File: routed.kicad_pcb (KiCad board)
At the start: 2 copper layers, 147.2 x 100.3 mm, 56 parts

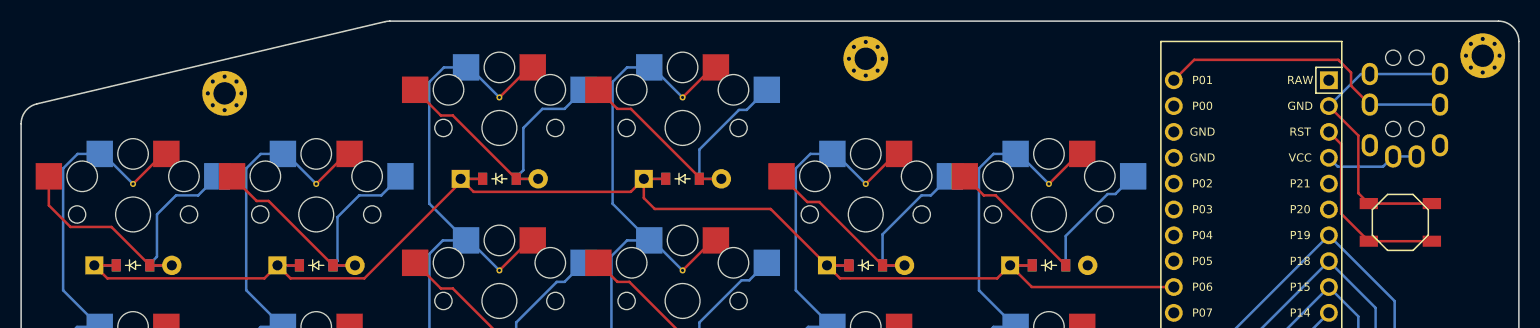
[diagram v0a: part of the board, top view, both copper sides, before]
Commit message: routed.kicad_pcb: fix trrs connections, unconnected diodes [bugfix]
Connected serial data pin P1 of Arduino to pin 2 of TRRS jack, rather
than pin 3 of TRRS jack. Using pin 2 for the serial data will allow
the use of both TRS and TRRS cables, whereas the former use of pin 3
would only work with TRRS cables.

Connect some diode pads that I forgot to connect (thanks, Design Rules
Checker).
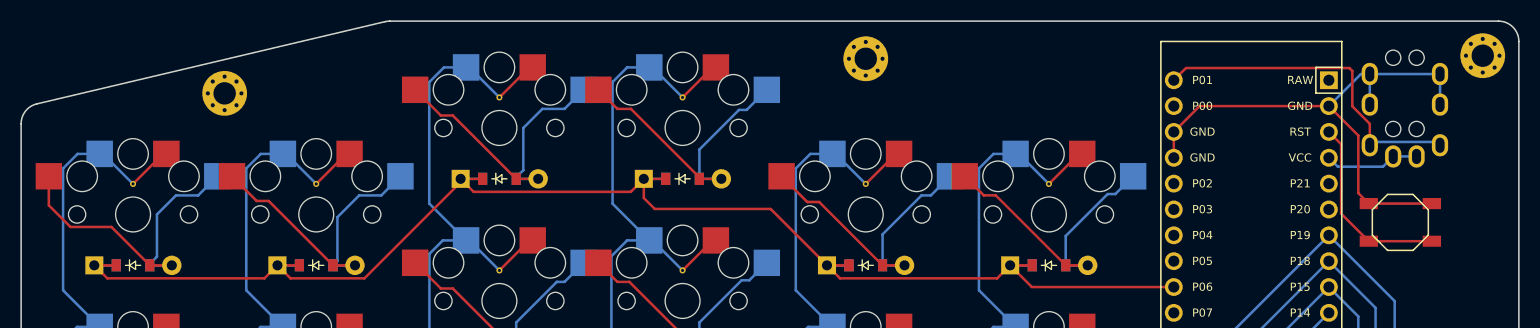
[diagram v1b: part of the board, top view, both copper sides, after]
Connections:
- TRRS1 pad 2: NA -> P1
- TRRS1 pad 3: P1 -> GND
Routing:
- net GND: track 29.6 -> 54.5 mm
- net inner_top: track 25.5 -> 29.8 mm
- net P1: track 29.6 -> 33.3 mm
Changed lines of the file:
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@@
   (net 36 "P5")
   (net 37 "P7")
-  (net 38 "NA")
   (footprint "E73:SW_TACT_ALPS_SKQGABE010" (layer "F.Cu")
     (at 192.286307 79.234243)
@@
     (at 193.8863 61.454246)
     (attr through_hole)
-    (fp_text reference "TRRS1" (at 0 14.2) (layer "Dwgs.User")
-      (effects (font (size 1 1) (thickness 0.15)))
-    )
-    (fp_text value "TRRS-PJ-320A-dual" (at 0 -5.6) (layer "F.Fab")
+    (fp_text reference "TRRS1" (at 6.399047 7.24677) (layer "Dwgs.User")
+      (effects (font (size 1 1) (thickness 0.15)))
+    )
+    (fp_text value "TRRS-PJ-320A-dual" (at 4.800308 12.920066 270) (layer "F.Fab") hide
       (effects (font (size 1 1) (thickness 0.15)))
     )
@@
     (fp_line (start -5.35 0) (end -5.35 12.1) (layer "Dwgs.User") (width 0.15))
     (fp_line (start 0.75 0) (end -5.35 0) (layer "Dwgs.User") (width 0.15))
-    (pad "" np_thru_hole circle locked (at -2.3 8.6) (size 1.5 1.5) (drill 1.5) (layers *.Cu *.Mask))
-    (pad "" np_thru_hole circle locked (at -2.3 1.6) (size 1.5 1.5) (drill 1.5) (layers *.Cu *.Mask))
-    (pad "" np_thru_hole circle locked (at 0 8.6) (size 1.5 1.5) (drill 1.5) (layers *.Cu *.Mask))
-    (pad "" np_thru_hole circle locked (at 0 1.6) (size 1.5 1.5) (drill 1.5) (layers *.Cu *.Mask))
-    (pad "1" thru_hole oval locked (at -2.3 11.3) (size 1.6 2.2) (drill oval 0.9 1.5) (layers *.Cu *.Mask)
+    (pad "" np_thru_hole circle (at -2.3 8.6) (size 1.5 1.5) (drill 1.5) (layers *.Cu *.Mask))
+    (pad "" np_thru_hole circle (at -2.3 1.6) (size 1.5 1.5) (drill 1.5) (layers *.Cu *.Mask))
+    (pad "" np_thru_hole circle (at 0 8.6) (size 1.5 1.5) (drill 1.5) (layers *.Cu *.Mask))
+    (pad "" np_thru_hole circle (at 0 1.6) (size 1.5 1.5) (drill 1.5) (layers *.Cu *.Mask))
+    (pad "1" thru_hole oval (at -2.3 11.3) (size 1.6 2.2) (drill oval 0.9 1.5) (layers *.Cu *.Mask)
       (net 28 "VCC"))
-    (pad "1" thru_hole oval locked (at 0 11.3) (size 1.6 2.2) (drill oval 0.9 1.5) (layers *.Cu *.Mask)
+    (pad "1" thru_hole oval (at 0 11.3) (size 1.6 2.2) (drill oval 0.9 1.5) (layers *.Cu *.Mask)
       (net 28 "VCC"))
-    (pad "2" thru_hole oval locked (at -4.6 10.2) (size 1.6 2.2) (drill oval 0.9 1.5) (layers *.Cu *.Mask)
-      (net 38 "NA"))
-    (pad "2" thru_hole oval locked (at 2.3 10.2) (size 1.6 2.2) (drill oval 0.9 1.5) (layers *.Cu *.Mask)
-      (net 38 "NA"))
-    (pad "3" thru_hole oval locked (at -4.6 6.2) (size 1.6 2.2) (drill oval 0.9 1.5) (layers *.Cu *.Mask)
+    (pad "2" thru_hole oval (at -4.6 10.2) (size 1.6 2.2) (drill oval 0.9 1.5) (layers *.Cu *.Mask)
       (net 31 "P1"))
-    (pad "3" thru_hole oval locked (at 2.3 6.2) (size 1.6 2.2) (drill oval 0.9 1.5) (layers *.Cu *.Mask)
+    (pad "2" thru_hole oval (at 2.3 10.2) (size 1.6 2.2) (drill oval 0.9 1.5) (layers *.Cu *.Mask)
       (net 31 "P1"))
-    (pad "4" thru_hole oval locked (at -4.6 3.2) (size 1.6 2.2) (drill oval 0.9 1.5) (layers *.Cu *.Mask)
+    (pad "3" thru_hole oval (at -4.6 6.2) (size 1.6 2.2) (drill oval 0.9 1.5) (layers *.Cu *.Mask)
       (net 26 "GND"))
-    (pad "4" thru_hole oval locked (at 2.3 3.2) (size 1.6 2.2) (drill oval 0.9 1.5) (layers *.Cu *.Mask)
+    (pad "3" thru_hole oval (at 2.3 6.2) (size 1.6 2.2) (drill oval 0.9 1.5) (layers *.Cu *.Mask)
+      (net 26 "GND"))
+    (pad "4" thru_hole oval (at -4.6 3.2) (size 1.6 2.2) (drill oval 0.9 1.5) (layers *.Cu *.Mask)
+      (net 26 "GND"))
+    (pad "4" thru_hole oval (at 2.3 3.2) (size 1.6 2.2) (drill oval 0.9 1.5) (layers *.Cu *.Mask)
       (net 26 "GND"))
   )
@@
   (gr_line (start 203.936299 61.454246) (end 203.936298 120.464232) (layer "Edge.Cuts") (width 0.15))
   (gr_arc (start 92.529629 59.50777) (mid 92.757869 59.467675) (end 92.989214 59.454245) (layer "Edge.Cuts") (width 0.15))
-  (gr_arc (start 56.756299 69.537017) (mid 57.18799 68.295877) (end 58.296716 67.590538) (layer "Edge.Cuts") (width 0.15))
+  (gr_arc (start 56.756299 69.537017) (mid 57.187989 68.295878) (end 58.296716 67.590538) (layer "Edge.Cuts") (width 0.15))
   (gr_line (start 175.092974 159.612011) (end 126.434172 136.759156) (layer "Edge.Cuts") (width 0.15))
-  (gr_arc (start 201.9363 59.454247) (mid 203.350515 60.040032) (end 203.936299 61.454246) (layer "Edge.Cuts") (width 0.15))
+  (gr_arc (start 201.9363 59.454247) (mid 203.350515 60.040031) (end 203.936299 61.454246) (layer "Edge.Cuts") (width 0.15))
   (gr_line (start 58.296716 67.590538) (end 92.529629 59.50777) (layer "Edge.Cuts") (width 0.15))
   (gr_line (start 126.392648 136.740234) (end 57.94761 106.480919) (layer "Edge.Cuts") (width 0.15))
@@
   (segment (start 160.106299 99.604248) (end 160.106297 95.452312) (width 0.25) (layer "B.Cu") (net 17))
   (segment (start 160.106297 95.452312) (end 161.979848 93.578763) (width 0.25) (layer "B.Cu") (net 17))
+  (segment (start 161.566301 83.454246) (end 159.406301 83.454246) (width 0.25) (layer "F.Cu") (net 18))
   (segment (start 151.355819 76.578762) (end 149.481299 74.704244) (width 0.25) (layer "F.Cu") (net 18))
   (segment (start 152.530822 76.578765) (end 151.355819 76.578762) (width 0.25) (layer "F.Cu") (net 18))
@@
   (segment (start 159.4063 80.571233) (end 163.529915 76.447618) (width 0.25) (layer "B.Cu") (net 18))
   (segment (start 164.287926 76.447618) (end 166.031298 74.704244) (width 0.25) (layer "B.Cu") (net 18))
+  (segment (start 161.566301 83.454246) (end 159.406301 83.454246) (width 0.25) (layer "B.Cu") (net 18))
   (segment (start 159.406302 83.454245) (end 159.4063 80.571233) (width 0.25) (layer "B.Cu") (net 18))
   (segment (start 142.142384 135.269978) (end 140.055984 134.710928) (width 0.25) (layer "F.Cu") (net 19))
@@
   (segment (start 154.255094 138.515567) (end 152.168696 137.956517) (width 0.25) (layer "B.Cu") (net 24))
   (segment (start 171.308444 147.37509) (end 169.781093 145.847737) (width 0.25) (layer "B.Cu") (net 24))
+  (segment (start 170.026296 70.344249) (end 172.566296 67.804249) (width 0.25) (layer "F.Cu") (net 26))
   (segment (start 189.186303 77.384248) (end 188.161782 76.359729) (width 0.25) (layer "F.Cu") (net 26))
+  (segment (start 172.566296 67.804249) (end 185.266296 67.804249) (width 0.25) (layer "F.Cu") (net 26))
   (segment (start 188.161782 76.359729) (end 188.161779 70.699727) (width 0.25) (layer "F.Cu") (net 26))
   (segment (start 189.186303 77.384248) (end 195.386304 77.384243) (width 0.25) (layer "F.Cu") (net 26))
+  (segment (start 170.026296 72.884249) (end 170.026296 70.344249) (width 0.25) (layer "F.Cu") (net 26))
   (segment (start 188.161779 70.699727) (end 185.266298 67.804245) (width 0.25) (layer "F.Cu") (net 26))
   (segment (start 189.286306 64.654244) (end 196.186302 64.654243) (width 0.25) (layer "B.Cu") (net 26))
   (segment (start 188.416298 64.65425) (end 185.266298 67.804245) (width 0.25) (layer "B.Cu") (net 26))
+  (segment (start 189.2863 64.654246) (end 189.2863 67.654246) (width 0.25) (layer "B.Cu") (net 26))
+  (segment (start 196.1863 64.654246) (end 196.1863 67.654246) (width 0.25) (layer "B.Cu") (net 26))
   (segment (start 189.286306 64.654244) (end 188.416298 64.65425) (width 0.25) (layer "B.Cu") (net 26))
   (segment (start 189.186303 81.084247) (end 186.467115 78.365056) (width 0.25) (layer "F.Cu") (net 27))
@@
   (segment (start 191.586301 72.754246) (end 193.8863 72.754247) (width 0.25) (layer "B.Cu") (net 28))
   (segment (start 190.580001 73.760544) (end 186.142602 73.760546) (width 0.25) (layer "B.Cu") (net 28))
-  (segment (start 187.446906 64.521718) (end 186.182561 63.257375) (width 0.25) (layer "F.Cu") (net 31))
-  (segment (start 189.286301 67.65425) (end 187.446912 65.81485) (width 0.25) (layer "F.Cu") (net 31))
-  (segment (start 186.182561 63.257375) (end 172.033177 63.257366) (width 0.25) (layer "F.Cu") (net 31))
-  (segment (start 187.446912 65.81485) (end 187.446906 64.521718) (width 0.25) (layer "F.Cu") (net 31))
-  (segment (start 172.033177 63.257366) (end 170.026301 65.264245) (width 0.25) (layer "F.Cu") (net 31))
-  (segment (start 189.286301 67.65425) (end 196.186297 67.654246) (width 0.25) (layer "B.Cu") (net 31))
+  (segment (start 189.2863 69.544557) (end 187.573292 67.831549) (width 0.25) (layer "F.Cu") (net 31))
+  (segment (start 189.2863 71.654246) (end 189.2863 69.544557) (width 0.25) (layer "F.Cu") (net 31))
+  (segment (start 187.573292 64.361084) (end 187.275646 64.063438) (width 0.25) (layer "F.Cu") (net 31))
+  (segment (start 187.275646 64.063438) (end 171.227107 64.063438) (width 0.25) (layer "F.Cu") (net 31))
+  (segment (start 187.573292 67.831549) (end 187.573292 64.361084) (width 0.25) (layer "F.Cu") (net 31))
+  (segment (start 171.227107 64.063438) (end 170.026296 65.264249) (width 0.25) (layer "F.Cu") (net 31))
+  (segment (start 189.2863 71.654246) (end 189.61082 71.329726) (width 0.25) (layer "B.Cu") (net 31))
+  (segment (start 195.86178 71.329726) (end 196.1863 71.654246) (width 0.25) (layer "B.Cu") (net 31))
+  (segment (start 189.61082 71.329726) (end 195.86178 71.329726) (width 0.25) (layer "B.Cu") (net 31))
 )

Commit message: board setup: set "solder mask clearance" to 0 [config]
In the File -> Board Setup dialog, change "solder mask clearance" from
0.05 -> 0.

I'm doing this because there was a warning in the File -> Fabrication
Outputs -> Gerbers dialog that told me I should do that.
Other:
- rule pad_to_mask_clearance: 0.05 -> 0
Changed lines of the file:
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@@
   )
   (setup
-    (pad_to_mask_clearance 0.05)
+    (stackup
+      (layer "F.SilkS" (type "Top Silk Screen"))
+      (layer "F.Paste" (type "Top Solder Paste"))
+      (layer "F.Mask" (type "Top Solder Mask") (thickness 0.01))
+      (layer "F.Cu" (type "copper") (thickness 0.035))
+      (layer "dielectric 1" (type "core") (thickness 1.51) (material "FR4") (epsilon_r 4.5) (loss_tangent 0.02))
+      (layer "B.Cu" (type "copper") (thickness 0.035))
+      (layer "B.Mask" (type "Bottom Solder Mask") (thickness 0.01))
+      (layer "B.Paste" (type "Bottom Solder Paste"))
+      (layer "B.SilkS" (type "Bottom Silk Screen"))
+      (copper_finish "None")
+      (dielectric_constraints no)
+    )
+    (pad_to_mask_clearance 0)
     (pcbplotparams
       (layerselection 0x00010fc_ffffffff)

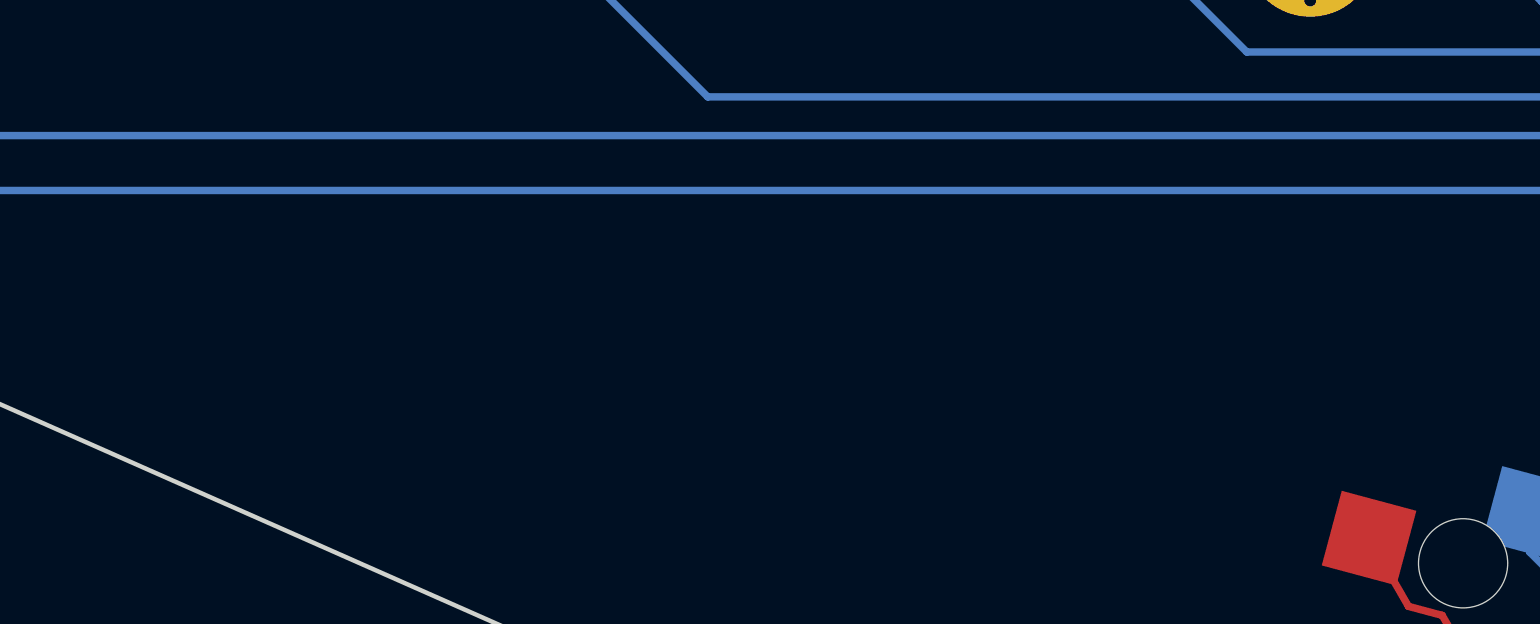
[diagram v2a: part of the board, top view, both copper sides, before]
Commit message: pcb: add "split-steno-kb 1.0.0" to silkscreen layer [feat]
Add a version number to the PCB, so I won't get confused if I end up
making multiple versions of the board.
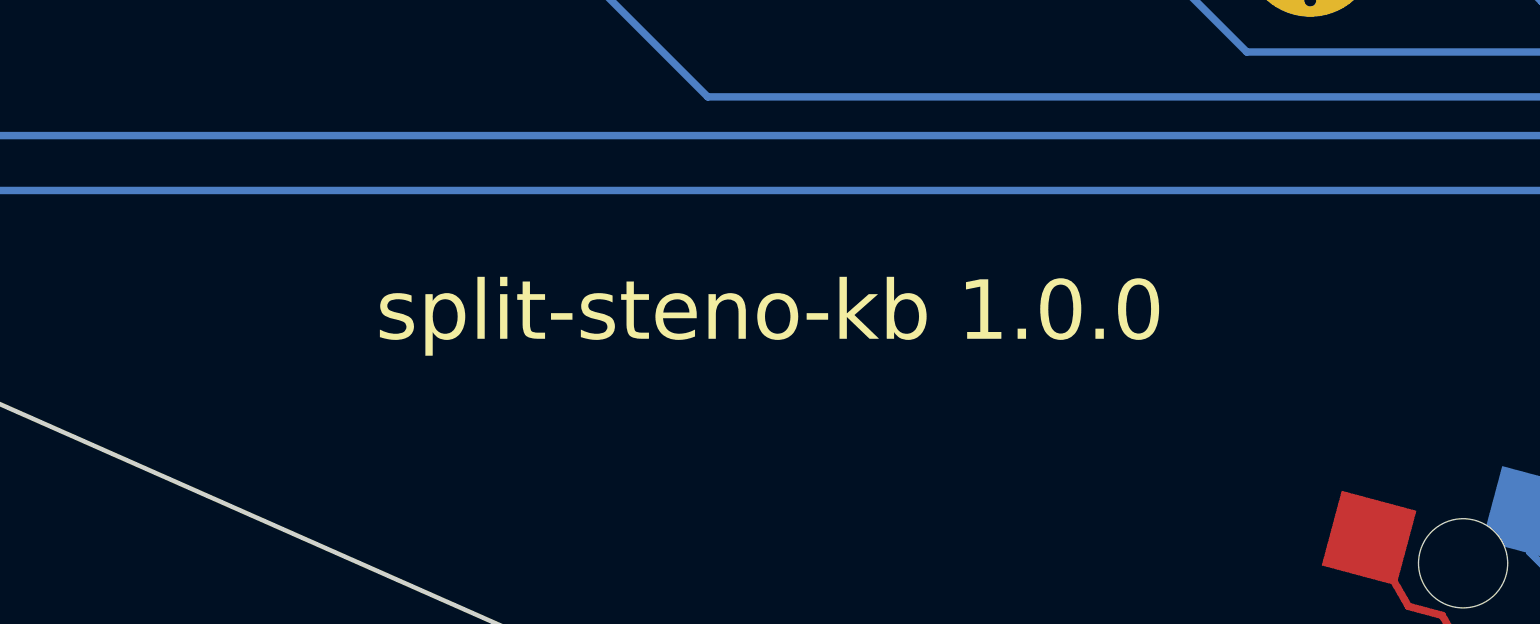
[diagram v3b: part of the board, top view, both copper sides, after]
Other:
- board text added: "split-steno-kb 1.0.0"
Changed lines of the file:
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@@
       (outputformat 1)
       (mirror false)
-      (drillshape 1)
+      (drillshape 0)
       (scaleselection 1)
-      (outputdirectory "")
+      (outputdirectory "gerbers/")
     )
   )
@@
   (gr_line (start 56.756302 104.651708) (end 56.756299 69.537017) (layer "Edge.Cuts") (width 0.15))
   (gr_arc (start 203.936302 120.464234) (mid 203.878848 120.940171) (end 203.709782 121.388761) (layer "Edge.Cuts") (width 0.15))
+  (gr_text "split-steno-kb 1.0.0" (at 112.583547 116.060323) (layer "F.SilkS")
+    (effects (font (size 2 2) (thickness 0.15)))
+  )
   (segment (start 71.031302 89.504248) (end 70.706297 89.504247) (width 0.25) (layer "F.Cu") (net 1))
   (segment (start 70.706297 89.504247) (end 67.756301 92.454247) (width 0.25) (layer "F.Cu") (net 1))
